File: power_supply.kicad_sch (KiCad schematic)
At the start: 0 parts

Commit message: Add components: TXS0108E, FT232 oscillators/power/USB, symbol library table
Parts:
- added C1, C10, C2, C29, C3, C31, C32, C33, C34, C35, C36, C4, C5, C6, C7, C8, C9: 100nf, Capacitor_SMD:C_0805_2012Metric, symbol Device:C
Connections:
- new net +3.3V: C1.1, C10.1, C2.1, C3.1, C4.1, C5.1, C6.1, C7.1, C8.1, C9.1
- new net +5V: C29.1, C31.1, C32.1, C33.1, C34.1, C35.1, C36.1
- new net GND: C1.2, C10.2, C2.2, C29.2, C3.2, C31.2, C32.2, C33.2, C34.2, C35.2, C36.2, C4.2, C5.2, C6.2, C7.2, C8.2, C9.2

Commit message: ESP32S3 branch initial changes
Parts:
- removed C3, C32, C33, C34, C35, C36, C4, C5, C6, C7, C8, C9: 100nf, Capacitor_SMD:C_0805_2012Metric, symbol Device:C
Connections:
- net +3.3V renamed +3V3
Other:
- moved on the sheet: C1, C10, C2, C29

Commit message: Update KiCad project files
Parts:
- removed C10: 100nf, Capacitor_SMD:C_0805_2012Metric, symbol Device:C
- added C28, C29, C30: 100nf, Capacitor_SMD:C_0805_2012Metric, symbol Device:C
- renumbered C1 to C25, C2 to C26, C29 to C31, C31 to C32
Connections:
- net +3V3: now also C28.1, C29.1, C30.1
- net GND: now also C28.2, C29.2, C30.2

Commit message: Remove unused schematic files, lock files, and backup directories
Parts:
- C25, C26, C28, C29, C30, C31, C32: footprint Capacitor_SMD:C_0805_2012Metric -> Capacitor_SMD:C_1206_3216Metric
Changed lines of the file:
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@@
 			)
 		)
-		(property "Footprint" "Capacitor_SMD:C_0805_2012Metric"
+		(property "Footprint" "Capacitor_SMD:C_1206_3216Metric"
 			(at 124.1552 134.62 0)
 			(hide yes)
@@
 			)
 		)
-		(property "Footprint" "Capacitor_SMD:C_0805_2012Metric"
+		(property "Footprint" "Capacitor_SMD:C_1206_3216Metric"
 			(at 138.1252 134.62 0)
 			(hide yes)
@@
 			)
 		)
-		(property "Footprint" "Capacitor_SMD:C_0805_2012Metric"
+		(property "Footprint" "Capacitor_SMD:C_1206_3216Metric"
 			(at 167.3352 95.25 0)
 			(hide yes)
@@
 			)
 		)
-		(property "Footprint" "Capacitor_SMD:C_0805_2012Metric"
+		(property "Footprint" "Capacitor_SMD:C_1206_3216Metric"
 			(at 152.0952 134.62 0)
 			(hide yes)
@@
 			)
 		)
-		(property "Footprint" "Capacitor_SMD:C_0805_2012Metric"
+		(property "Footprint" "Capacitor_SMD:C_1206_3216Metric"
 			(at 103.8352 93.98 0)
 			(hide yes)
@@
 			)
 		)
-		(property "Footprint" "Capacitor_SMD:C_0805_2012Metric"
+		(property "Footprint" "Capacitor_SMD:C_1206_3216Metric"
 			(at 181.3052 95.25 0)
 			(hide yes)
@@
 			)
 		)
-		(property "Footprint" "Capacitor_SMD:C_0805_2012Metric"
+		(property "Footprint" "Capacitor_SMD:C_1206_3216Metric"
 			(at 89.8652 93.98 0)
 			(hide yes)

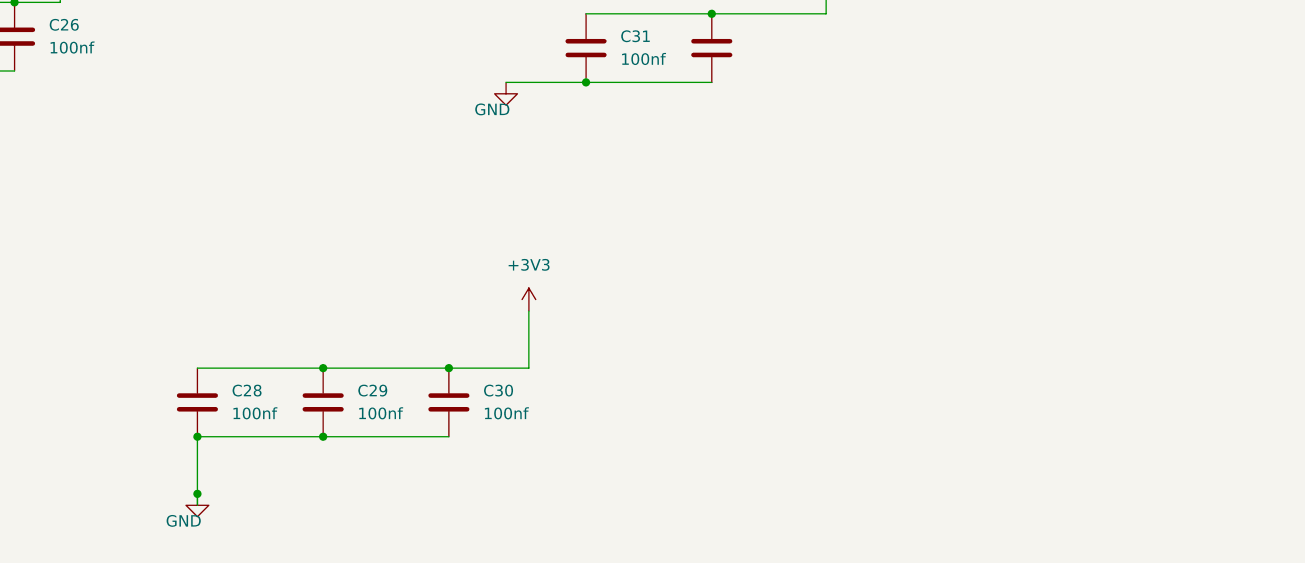
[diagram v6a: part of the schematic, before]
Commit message: Actualización de esquema y PCB del proyecto ESP32C6 Xiaozhi
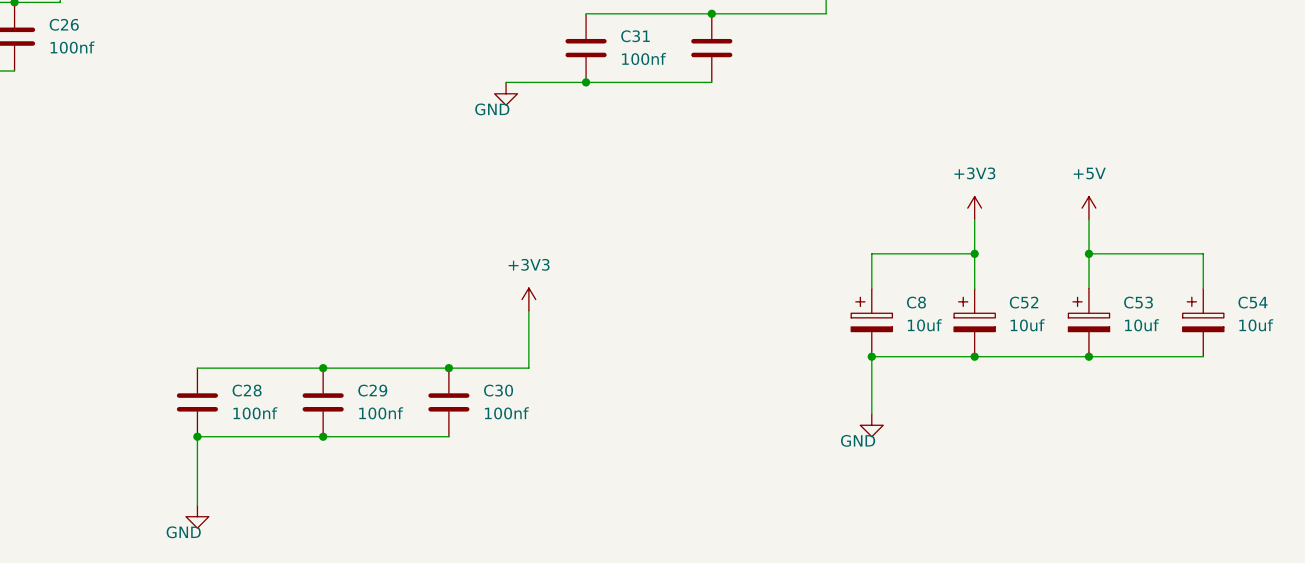
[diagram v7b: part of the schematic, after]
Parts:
- added C52, C53, C54, C8: 10uf, Capacitor_SMD:C_Elec_6.3x7.7, symbol Device:C_Polarized
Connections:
- net +3V3: now also C52.1, C8.1
- net +5V: now also C53.1, C54.1
- net GND: now also C52.2, C53.2, C54.2, C8.2

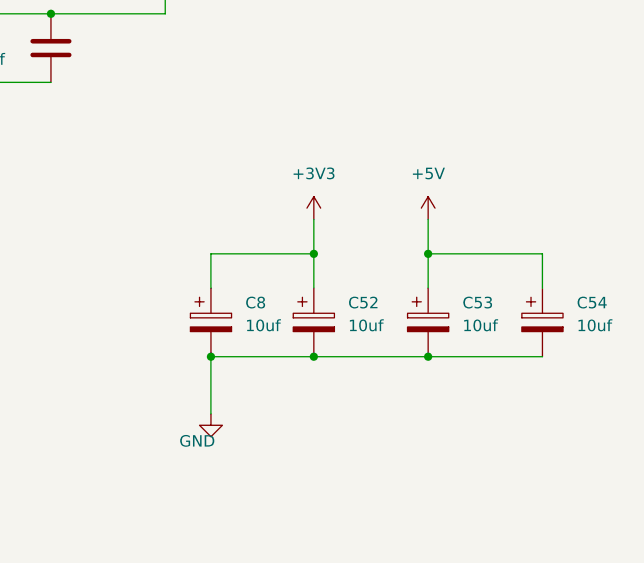
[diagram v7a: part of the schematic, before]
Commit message: Actualizaciones para versión single ESP32C6
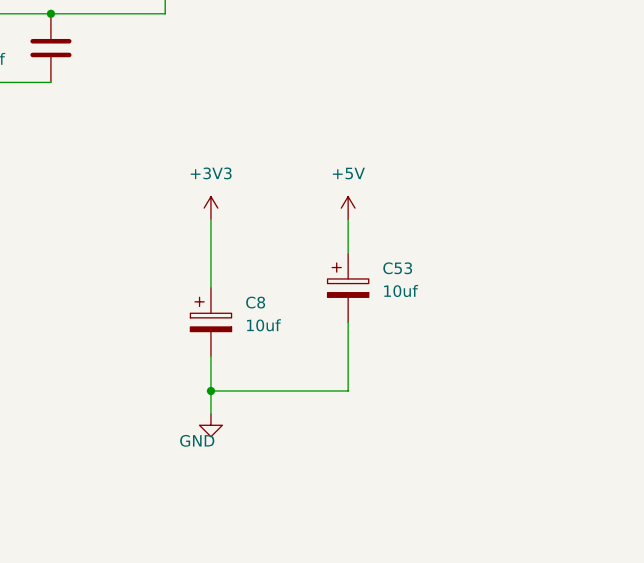
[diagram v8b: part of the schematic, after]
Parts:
- removed C52, C54: 10uf, Capacitor_SMD:C_Elec_6.3x7.7, symbol Device:C_Polarized
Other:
- moved on the sheet: C53
